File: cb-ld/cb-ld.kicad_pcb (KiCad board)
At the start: 4 copper layers, 31.7 x 56.6 mm, 37 parts, among them P1 CONN_01X14, P2 CONN_01X14, U1 MBC13917, U4 CC1190

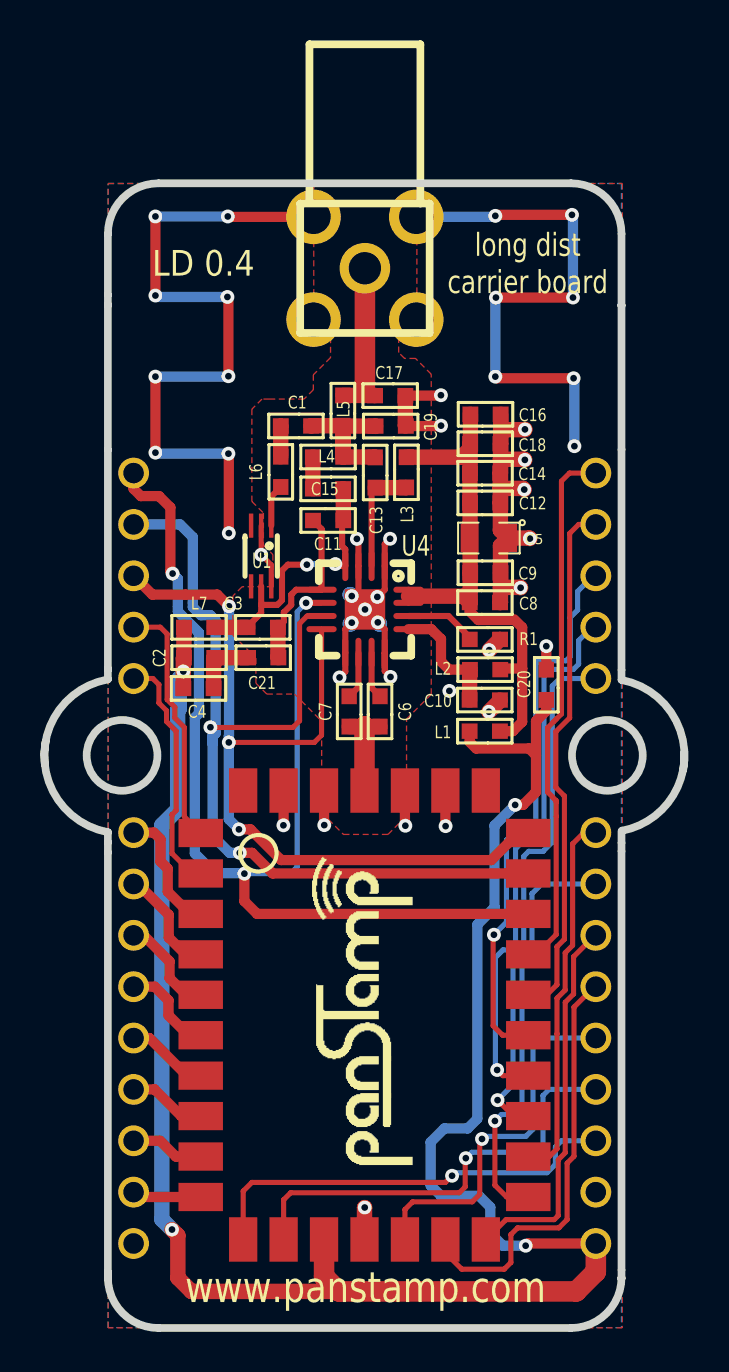
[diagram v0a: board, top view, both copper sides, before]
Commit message: External LNA removed from design
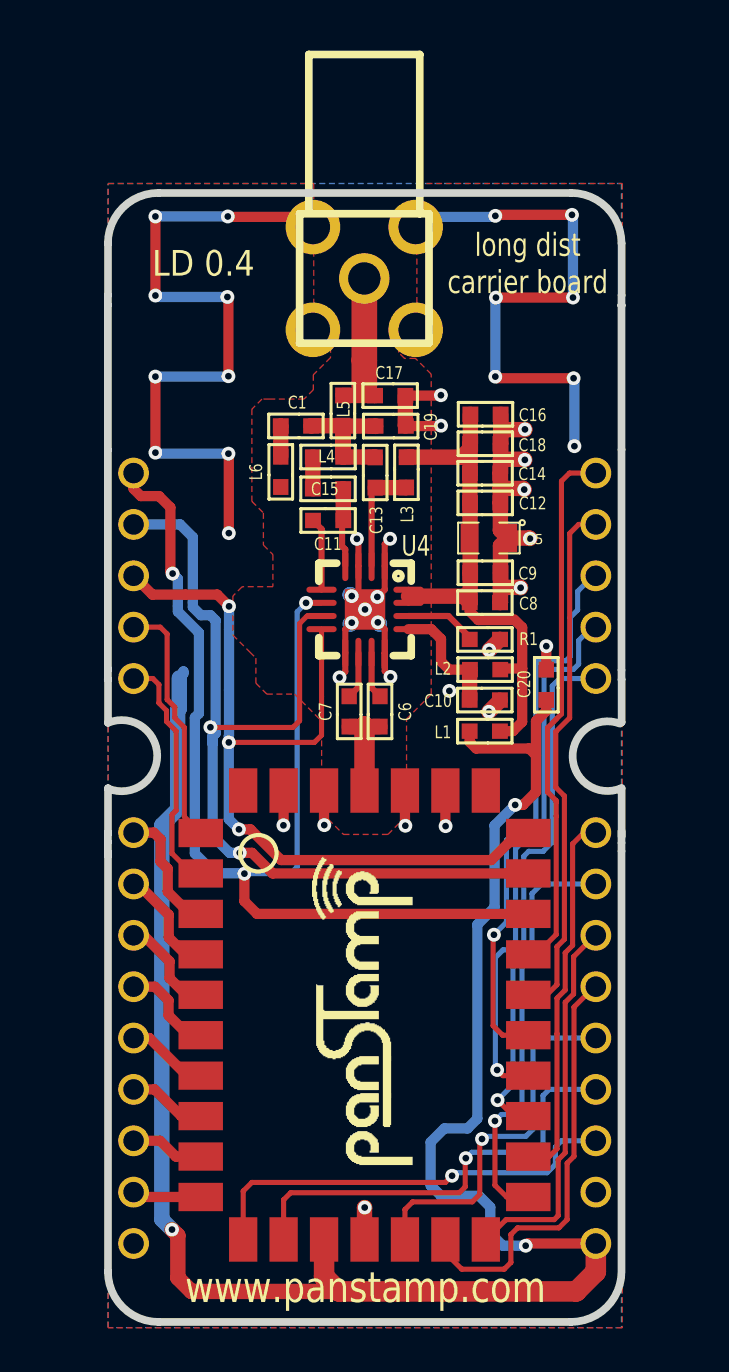
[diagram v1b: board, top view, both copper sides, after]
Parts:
- removed C2: 47p, mysmd:SM0603S
- removed C21: 3p, mysmd:SM0603S
- removed C3: 2p, mysmd:SM0603S
- removed C4: 0.1u, mysmd:SM0603S
- removed L7: 10n, mysmd:SM0603S
- removed U1: MBC13917, mysmd:MLPD-6
- moved ANT1 0.51 mm to (197.3, 49.5)
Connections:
- net /LNA_B renamed Net-(C11-Pad1)
- net /LNA_C renamed Net-(C11-Pad2)
- C13 pad 1: /LNA_A -> Net-(C13-Pad1)
- C19 pad 1: /LNA_A -> Net-(C13-Pad1)
- L4 pad 2: /LNA_A -> Net-(C13-Pad1)
- L5 pad 2: /LNA_A -> Net-(C13-Pad1)
- U4 pad 17: GND -> (no net)
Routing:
- net Net-(C11-Pad1): track 15.0 -> 4.15 mm, vias 2 -> 0
- net GND: track 119.5 -> 113.0 mm, vias 41 -> 40
- net Net-(C13-Pad1): track 0.00 -> 6.33 mm
- net /LNA_A: track 7.90 -> 1.58 mm
- net Net-(C11-Pad2): track 8.98 -> 3.60 mm
- net VCC: track 101.0 -> 98.0 mm, vias 4 -> 3
- net Net-(L6-Pad2): track 2.11 -> 0.00 mm
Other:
- board size 31.7 x 56.6 mm -> 25.4 x 55.8 mm

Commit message: Comments updated
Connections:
- U4 pad 17: (no net) -> GND
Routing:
- net /LNA_A: track 1.58 -> 0.02 mm
- net Net-(C13-Pad1): track 6.33 -> 4.78 mm
- net Net-(ANT1-Pad1): track 8.24 -> 9.46 mm
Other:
- rule trace_min: 0.1524 -> 3.87096
- rule via_min_size: 0.6858 -> 17.41932
- board text added: "LD 1.0"
- board text removed: "LD 0.4"
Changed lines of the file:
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@@
-(kicad_pcb (version 4) (host pcbnew 0.201507042246+5884~23~ubuntu14.04.1-product)
+(kicad_pcb (version 4) (host pcbnew 0.201510060346+6247~30~ubuntu14.04.1-product)
   (general
-    (links 89)
-    (no_connects 6)
-    (area 181.284044 45.054499 213.325275 101.270501)
+    (links 90)
+    (no_connects 0)
+    (area 182.12525 38.057699 212.49585 101.370001)
     (thickness 1.6002)
     (drawings 65)
@@
     (title "USB carrier board for panStamp, aka panStick")
     (date "25 Feb 2015")
-    (rev 4.0)
+    (rev 1.0)
     (company panStamp)
   )
@@
     (zone_clearance 0.1524)
     (zone_45_only yes)
-    (trace_min 0.1524)
+    (trace_min 3.87096)
     (segment_width 0.381)
     (edge_width 0.381)
     (via_size 0.6858)
     (via_drill 0.3302)
-    (via_min_size 0.6858)
+    (via_min_size 17.41932)
     (via_min_drill 0.3302)
     (user_via 0.6096 0.1016)
@@
     (user_via 0.6858 0.3302)
     (user_via 0.8763 0.3683)
-    (uvia_size 0.5588)
-    (uvia_drill 0.254)
+    (uvia_size 0.6858)
+    (uvia_drill 0.3302)
     (uvias_allowed no)
-    (uvia_min_size 0.508)
+    (uvia_min_size 12.9032)
     (uvia_min_drill 0.254)
     (pcb_text_width 0.3048)
@@
     (mod_text_size 1.524 1.524)
     (mod_text_width 0.3048)
-    (pad_size 2 2)
+    (pad_size 1.50076 0.3)
     (pad_drill 0)
     (pad_to_mask_clearance 0)
@@
     (visible_elements FFFFF7BF)
     (pcbplotparams
-      (layerselection 0x010f0_80000001)
+      (layerselection 0x010f8_80000001)
       (usegerberextensions true)
       (excludeedgelayer true)
@@
     (via_dia 0.6858)
     (via_drill 0.3302)
-    (uvia_dia 0.5588)
-    (uvia_drill 0.254)
+    (uvia_dia 0.6858)
+    (uvia_drill 0.3302)
     (add_net /D0)
     (add_net /D1)
@@
   )
   (module SM0603S (layer Front)
-    (at 196.24 56.01 270)
+    (at 196.26834 56.007 270)
     (attr smd)
     (fp_text reference L5 (at -0.07636 -0.0356 270) (layer F.SilkS)
@@
     (pad 16 smd oval (at -0.975 -2.14962) (size 1.50076 0.3) (layers Front F.Paste F.Mask)
       (net 4 "Net-(C12-Pad2)") (solder_paste_margin -0.025))
-    (pad 17 smd rect (at 0 0) (size 2 2) (layers Front F.Paste F.Mask))
+    (pad 17 smd rect (at 0 0) (size 2 2) (layers Front F.Paste F.Mask)
+      (net 2 GND) (solder_paste_margin_ratio -0.2))
   )
   (module mysmd:PANSTAMP_2 (layer Front)
@@
   (gr_line (start 184.62 77.84) (end 184.62 77.36) (angle 90) (layer Edge.Cuts) (width 0.381))
   (gr_line (start 210.02 98.5) (end 210.02 77.81) (angle 90) (layer Edge.Cuts) (width 0.381))
-  (gr_text "LD 0.4" (at 189.34 48.75) (layer F.SilkS)
+  (gr_text "LD 1.0" (at 205.24724 49.50968) (layer F.SilkS)
     (effects (font (size 1.27 1.143) (thickness 0.1524)))
   )
-  (gr_text "long dist\ncarrier board" (at 205.38 48.75) (layer F.SilkS)
+  (gr_text "long dist\ncarrier board" (at 188.37148 51.9684 90) (layer F.SilkS)
     (effects (font (size 1.143 0.889) (thickness 0.1524)))
   )
@@
   (segment (start 199.3724 59.82122) (end 199.38256 59.81106) (width 0.762) (layer Front) (net 9))
   (segment (start 194.75722 58.30484) (end 194.75722 59.87964) (width 0.762) (layer Front) (net 10))
+  (segment (start 196.26834 55.2577) (end 196.8673 55.2577) (width 0.508) (layer Front) (net 11))
+  (segment (start 196.8673 55.2577) (end 197.3 54.825) (width 0.508) (layer Front) (net 11))
   (segment (start 197.3 53.525) (end 197.3 54.825) (width 0.762) (layer Front) (net 11))
   (segment (start 197.3 53.525) (end 197.3 54.825) (width 1.27) (layer Front) (net 11))
@@
   (segment (start 199.69 95.14) (end 202.64 95.14) (width 0.254) (layer Front) (net 35))
   (segment (start 199.31 95.52) (end 199.69 95.14) (width 0.254) (layer Front) (net 35))
-  (segment (start 196.24 56.7593) (end 194.68 56.7593) (width 0.762) (layer Front) (net 36))
   (segment (start 194.68 56.7593) (end 194.6693 56.77) (width 0.762) (layer Front) (net 36))
   (segment (start 203.31 97) (end 203.33 97) (width 0.254) (layer Front) (net 38))
@@
   (segment (start 196.2609 59.88472) (end 196.25582 59.87964) (width 0.762) (layer Front) (net 41))
   (segment (start 196.36032 61.5437) (end 196.2609 61.44428) (width 0.3048) (layer Front) (net 41))
-  (segment (start 196.25582 58.30484) (end 196.25582 56.77512) (width 0.762) (layer Front) (net 42))
-  (segment (start 196.25582 56.77512) (end 196.24 56.7593) (width 0.762) (layer Front) (net 42))
-  (segment (start 196.24566 56.7656) (end 196.24566 58.29468) (width 0.762) (layer Front) (net 42))
+  (segment (start 196.26834 56.7563) (end 196.26834 58.29232) (width 0.762) (layer Front) (net 42))
+  (segment (start 196.26834 58.29232) (end 196.25582 58.30484) (width 0.762) (layer Front) (net 42))
+  (segment (start 196.26834 56.7563) (end 197.83656 56.7563) (width 0.762) (layer Front) (net 42))
+  (segment (start 197.83656 56.7563) (end 197.85602 56.77576) (width 0.762) (layer Front) (net 42))
   (segment (start 196.24566 58.29468) (end 196.25582 58.30484) (width 0.762) (layer Front) (net 42))
-  (segment (start 197.85602 56.77576) (end 196.25582 56.77576) (width 0.762) (layer Front) (net 42))
-  (segment (start 196.25582 56.77576) (end 196.24566 56.7656) (width 0.762) (layer Front) (net 42))
   (segment (start 197.83824 56.79354) (end 197.85602 56.77576) (width 0.762) (layer Front) (net 42))
   (segment (start 196.25582 58.30484) (end 197.82046 58.30484) (width 0.762) (layer Front) (net 42))
@@
     (connect_pads (clearance 0.1524))
     (min_thickness 0.254)
-    (fill (arc_segments 16) (thermal_gap 0.508) (thermal_bridge_width 0.508))
+    (fill yes (arc_segments 16) (thermal_gap 0.508) (thermal_bridge_width 0.508))
     (polygon
       (pts
